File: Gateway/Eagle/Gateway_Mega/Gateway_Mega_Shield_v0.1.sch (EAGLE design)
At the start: 10 parts

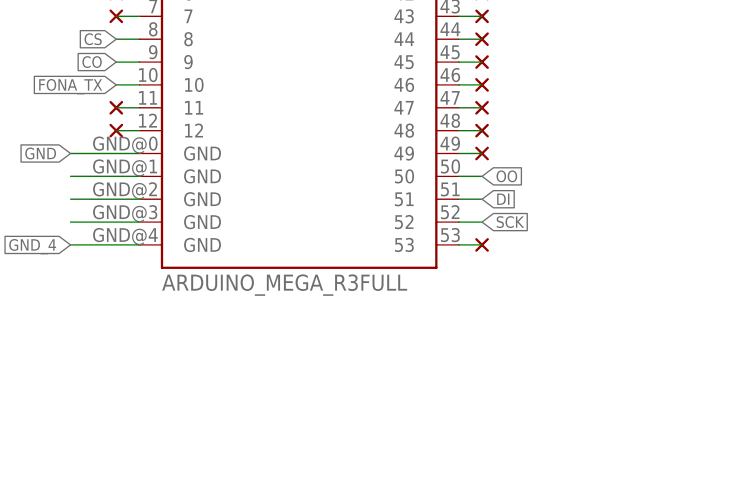
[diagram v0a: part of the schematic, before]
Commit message: Modify sparkfun arduino mega shield
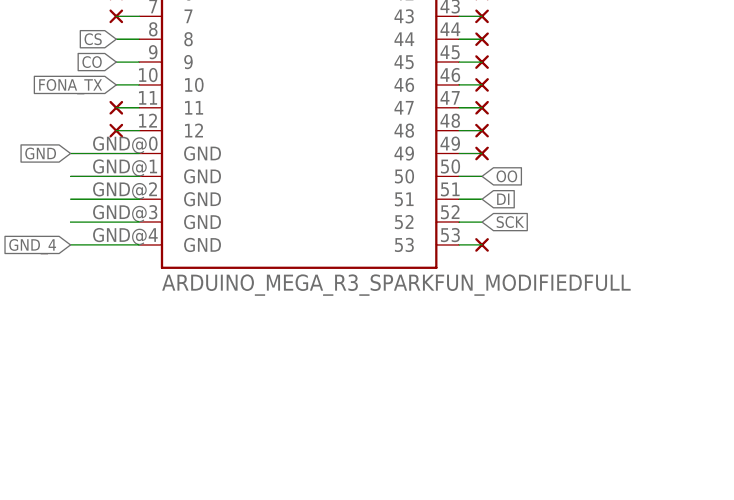
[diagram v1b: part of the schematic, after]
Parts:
- B1: value ARDUINO_MEGA_R3FULL -> ARDUINO_MEGA_R3_SPARKFUN_MODIFIEDFULL; device SparkFun-Boards:ARDUINO_MEGA_R3FULL -> wsn_x:ARDUINO_MEGA_R3_SPARKFUN_MODIFIEDFULL
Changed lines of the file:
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@@
 <parts>
 <part name="FRAME1" library="frames" library_urn="urn:adsk.eagle:library:229" deviceset="DINA4_L" device=""/>
-<part name="B1" library="SparkFun-Boards" library_urn="urn:adsk.eagle:library:509" deviceset="ARDUINO_MEGA_R3" device="FULL" package3d_urn="urn:adsk.eagle:package:37320/1"/>
+<part name="B1" library="wsn_x" deviceset="ARDUINO_MEGA_R3_SPARKFUN_MODIFIED" device="FULL"/>
 <part name="LED1" library="adafruit" library_urn="urn:adsk.eagle:library:420" deviceset="LED" device="5MM" package3d_urn="urn:adsk.eagle:package:6240538/1"/>
 <part name="R1" library="adafruit" library_urn="urn:adsk.eagle:library:420" deviceset="R-US_" device="0207/10" package3d_urn="urn:adsk.eagle:package:6240597/1"/>
